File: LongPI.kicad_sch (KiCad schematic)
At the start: 10 parts, among them J1 USB_C_Receptacle_USB2.0, J2 Conn_01x30, U1 RP2040, U2 USBLC6-2SC6, U3 XC6210B332MR, U4 W25Q128JVS

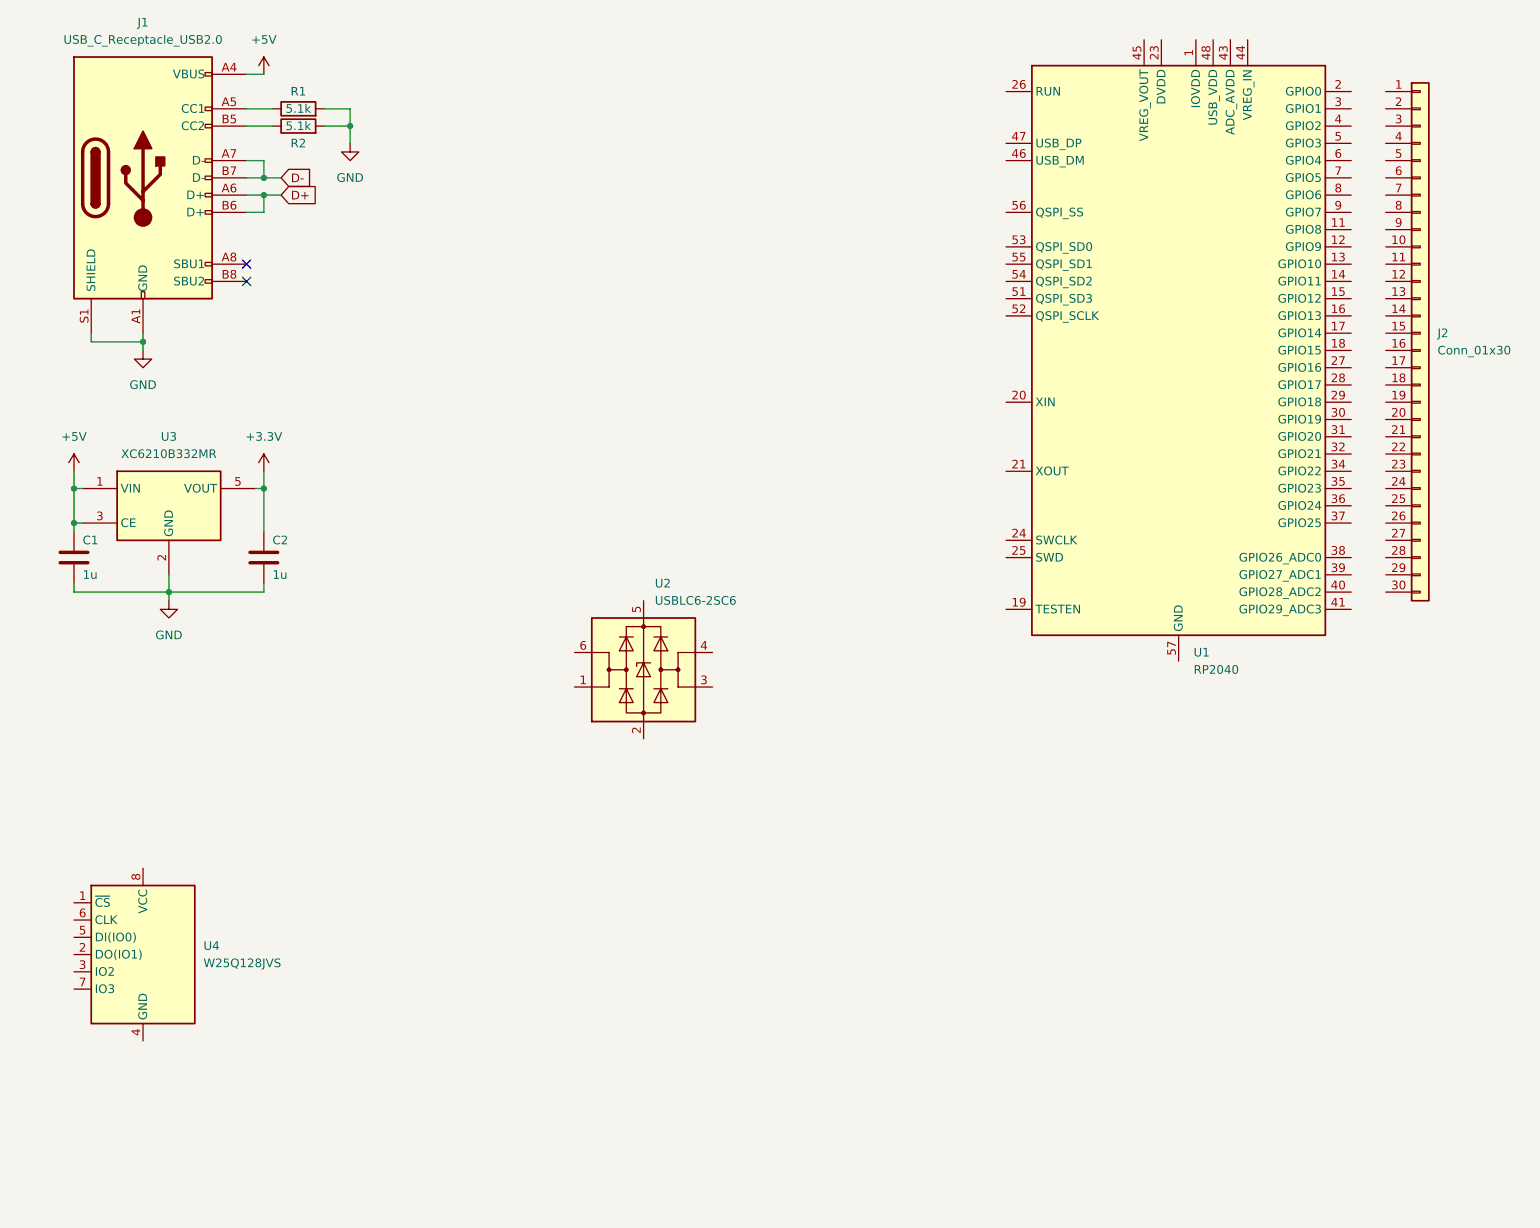
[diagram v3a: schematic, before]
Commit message: ESD protection setup on sch
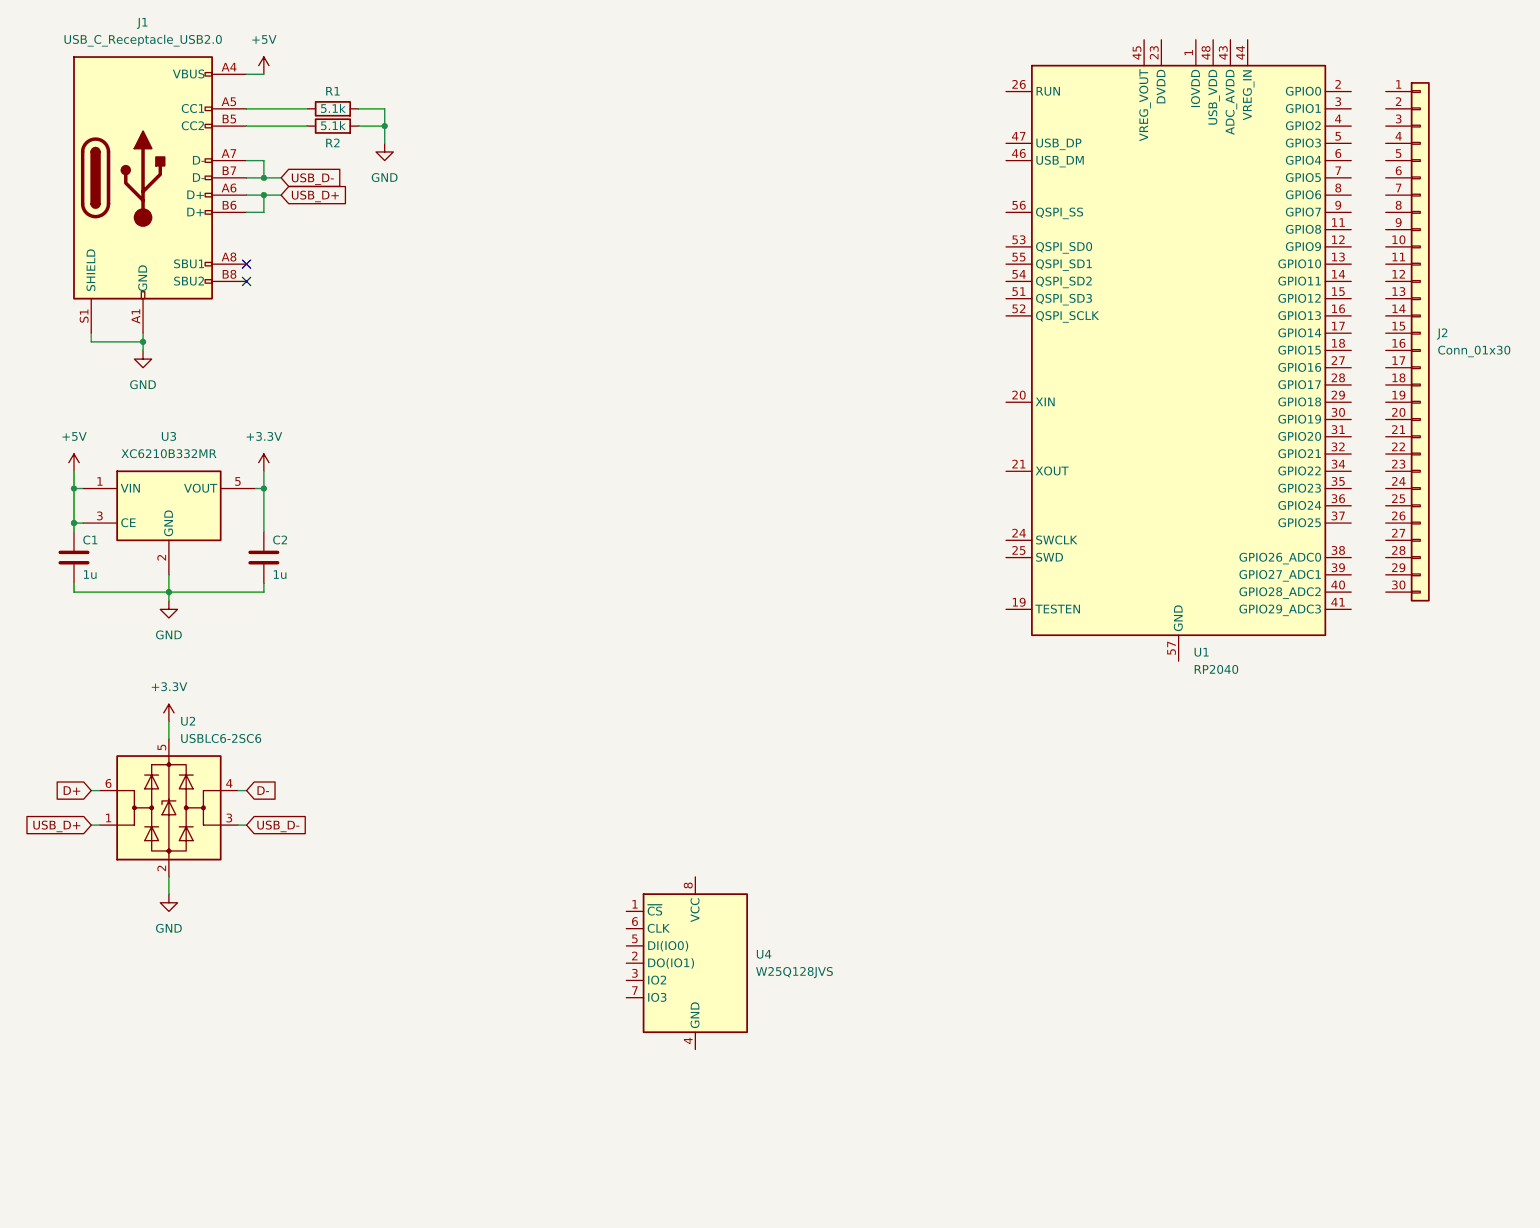
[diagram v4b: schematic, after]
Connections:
- net +3.3V: now also U2.5 (VBUS)
- net D+: now also U2.6 (I/O1); no longer J1.A6 (D+), J1.B6 (D+)
- net D-: now also U2.4 (I/O2); no longer J1.A7 (D-), J1.B7 (D-)
- net GND: now also U2.2 (GND)
- net USB_D+: now reaches U2.1 (I/O1)
- net USB_D+: now also J1.A6 (D+), J1.B6 (D+)
- net USB_D-: now reaches U2.3 (I/O2)
- net USB_D-: now also J1.A7 (D-), J1.B7 (D-)
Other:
- moved on the sheet: R1, R2, U2, U4

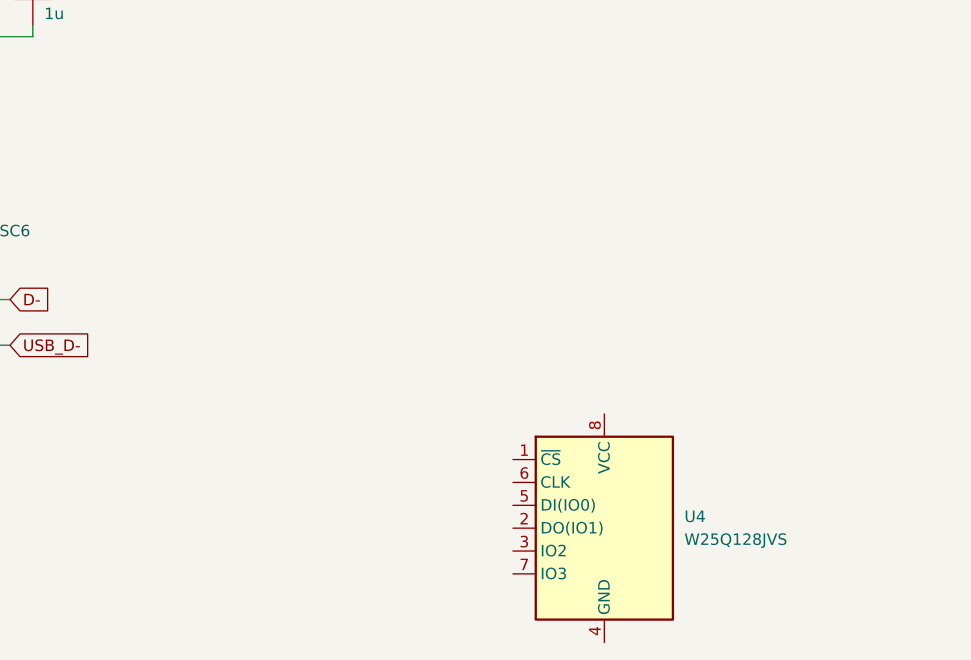
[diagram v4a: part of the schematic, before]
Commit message: Flash setup on sch
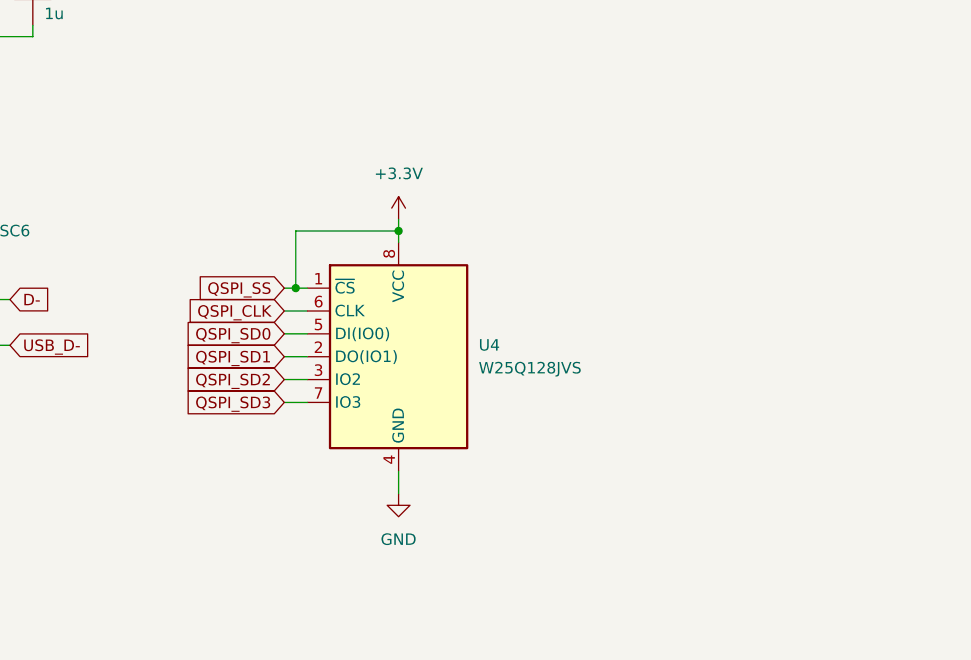
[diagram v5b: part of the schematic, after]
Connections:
- net +3.3V: now also U4.1 (~{CS}), U4.8 (VCC)
- net GND: now also U4.4 (GND)
- net QSPI_SD1: now reaches U4.2 (DO(IO1))
- net QSPI_SD2: now reaches U4.3 (IO2)
- net QSPI_SD0: now reaches U4.5 (DI(IO0))
- net QSPI_CLK: now reaches U4.6 (CLK)
- net QSPI_SD3: now reaches U4.7 (IO3)
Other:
- moved on the sheet: U4
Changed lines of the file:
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@@
   (junction (at 53.34 39.37) (diameter 0) (color 0 0 0 0)
   )
+  (junction (at 82.55 128.27) (diameter 0) (color 0 0 0 0)
+  )
   (junction (at 35.56 63.5) (diameter 0) (color 0 0 0 0)
   )
@@
   )
   (junction (at 53.34 85.09) (diameter 0) (color 0 0 0 0)
+  )
+  (junction (at 93.98 121.92) (diameter 0) (color 0 0 0 0)
   )
   (junction (at 71.12 31.75) (diameter 0) (color 0 0 0 0)
@@
     (stroke (width 0) (type default))
   )
+  (wire (pts (xy 82.55 128.27) (xy 83.82 128.27))
+    (stroke (width 0) (type default))
+  )
   (wire (pts (xy 50.8 44.45) (xy 53.34 44.45))
     (stroke (width 0) (type default))
@@
     (stroke (width 0) (type default))
   )
+  (wire (pts (xy 81.28 138.43) (xy 83.82 138.43))
+    (stroke (width 0) (type default))
+  )
   (wire (pts (xy 53.34 85.09) (xy 52.07 85.09))
     (stroke (width 0) (type default))
@@
     (stroke (width 0) (type default))
   )
+  (wire (pts (xy 81.28 128.27) (xy 82.55 128.27))
+    (stroke (width 0) (type default))
+  )
   (wire (pts (xy 25.4 91.44) (xy 25.4 90.17))
     (stroke (width 0) (type default))
@@
     (stroke (width 0) (type default))
   )
+  (wire (pts (xy 81.28 133.35) (xy 83.82 133.35))
+    (stroke (width 0) (type default))
+  )
+  (wire (pts (xy 81.28 135.89) (xy 83.82 135.89))
+    (stroke (width 0) (type default))
+  )
   (wire (pts (xy 50.8 39.37) (xy 53.34 39.37))
     (stroke (width 0) (type default))
@@
     (stroke (width 0) (type default))
   )
+  (wire (pts (xy 81.28 140.97) (xy 83.82 140.97))
+    (stroke (width 0) (type default))
+  )
   (wire (pts (xy 49.53 134.62) (xy 50.8 134.62))
     (stroke (width 0) (type default))
@@
     (stroke (width 0) (type default))
   )
+  (wire (pts (xy 93.98 120.65) (xy 93.98 121.92))
+    (stroke (width 0) (type default))
+  )
   (wire (pts (xy 50.8 31.75) (xy 59.69 31.75))
     (stroke (width 0) (type default))
@@
     (stroke (width 0) (type default))
   )
+  (wire (pts (xy 93.98 148.59) (xy 93.98 151.13))
+    (stroke (width 0) (type default))
+  )
   (wire (pts (xy 67.31 31.75) (xy 71.12 31.75))
     (stroke (width 0) (type default))
   )
+  (wire (pts (xy 81.28 130.81) (xy 83.82 130.81))
+    (stroke (width 0) (type default))
+  )
   (wire (pts (xy 39.37 119.38) (xy 39.37 121.92))
     (stroke (width 0) (type default))
@@
     (stroke (width 0) (type default))
   )
+  (wire (pts (xy 93.98 121.92) (xy 82.55 121.92))
+    (stroke (width 0) (type default))
+  )
+  (wire (pts (xy 93.98 121.92) (xy 93.98 123.19))
+    (stroke (width 0) (type default))
+  )
   (wire (pts (xy 25.4 100.33) (xy 39.37 100.33))
     (stroke (width 0) (type default))
@@
     (stroke (width 0) (type default))
   )
+  (wire (pts (xy 82.55 121.92) (xy 82.55 128.27))
+    (stroke (width 0) (type default))
+  )
   (wire (pts (xy 50.8 36.83) (xy 53.34 36.83))
     (stroke (width 0) (type default))
+  )
+  (global_label "QSPI_CLK" (shape input) (at 81.28 130.81 180) (fields_autoplaced)
+    (effects (font (size 1.27 1.27)) (justify right))
+    (property "Intersheetrefs" "${INTERSHEET_REFS}" (at 69.3443 130.81 0)
+      (effects (font (size 1.27 1.27)) (justify right) hide)
+    )
   )
   (global_label "D-" (shape input) (at 50.8 129.54 0) (fields_autoplaced)
@@
     )
   )
+  (global_label "QSPI_SD2" (shape input) (at 81.28 138.43 180) (fields_autoplaced)
+    (effects (font (size 1.27 1.27)) (justify right))
+    (property "Intersheetrefs" "${INTERSHEET_REFS}" (at 69.2234 138.43 0)
+      (effects (font (size 1.27 1.27)) (justify right) hide)
+    )
+  )
+  (global_label "QSPI_SD1" (shape input) (at 81.28 135.89 180) (fields_autoplaced)
+    (effects (font (size 1.27 1.27)) (justify right))
+    (property "Intersheetrefs" "${INTERSHEET_REFS}" (at 69.2234 135.89 0)
+      (effects (font (size 1.27 1.27)) (justify right) hide)
+    )
+  )
+  (global_label "QSPI_SD0" (shape input) (at 81.28 133.35 180) (fields_autoplaced)
+    (effects (font (size 1.27 1.27)) (justify right))
+    (property "Intersheetrefs" "${INTERSHEET_REFS}" (at 69.2234 133.35 0)
+      (effects (font (size 1.27 1.27)) (justify right) hide)
+    )
+  )
   (global_label "USB_D+" (shape input) (at 27.94 134.62 180) (fields_autoplaced)
     (effects (font (size 1.27 1.27)) (justify right))
@@
     )
   )
+  (global_label "QSPI_SD3" (shape input) (at 81.28 140.97 180) (fields_autoplaced)
+    (effects (font (size 1.27 1.27)) (justify right))
+    (property "Intersheetrefs" "${INTERSHEET_REFS}" (at 69.2234 140.97 0)
+      (effects (font (size 1.27 1.27)) (justify right) hide)
+    )
+  )
+  (global_label "QSPI_SS" (shape input) (at 81.28 128.27 180) (fields_autoplaced)
+    (effects (font (size 1.27 1.27)) (justify right))
+    (property "Intersheetrefs" "${INTERSHEET_REFS}" (at 70.4934 128.27 0)
+      (effects (font (size 1.27 1.27)) (justify right) hide)
+    )
+  )
   (global_label "USB_D-" (shape input) (at 55.88 39.37 0) (fields_autoplaced)
     (effects (font (size 1.27 1.27)) (justify left))
@@
     )
   )
+  (symbol (lib_id "power:+3.3V") (at 93.98 120.65 0) (unit 1)
+    (in_bom yes) (on_board yes) (dnp no) (fields_autoplaced)
+    (property "Reference" "#PWR09" (at 93.98 124.46 0)
+      (effects (font (size 1.27 1.27)) hide)
+    )
+    (property "Value" "+3.3V" (at 93.98 115.57 0)
+      (effects (font (size 1.27 1.27)))
+    )
+    (property "Footprint" "" (at 93.98 120.65 0)
+      (effects (font (size 1.27 1.27)) hide)
+    )
+    (property "Datasheet" "" (at 93.98 120.65 0)
+      (effects (font (size 1.27 1.27)) hide)
+    )
+    (pin "1")
+    (instances
+      (project "LongPI"
+        (path "/cc33761c-f139-4a76-bdf7-f72d959ddb3d"
+          (reference "#PWR09") (unit 1)
+        )
+      )
+    )
+  )
   (symbol (lib_id "power:+5V") (at 25.4 82.55 0) (unit 1)
     (in_bom yes) (on_board yes) (dnp no) (fields_autoplaced)
@@
     )
   )
-  (symbol (lib_id "Memory_Flash:W25Q128JVS") (at 116.84 154.94 0) (unit 1)
-    (in_bom yes) (on_board yes) (dnp no) (fields_autoplaced)
-    (property "Reference" "U4" (at 125.73 153.67 0)
-      (effects (font (size 1.27 1.27)) (justify left))
-    )
-    (property "Value" "W25Q128JVS" (at 125.73 156.21 0)
-      (effects (font (size 1.27 1.27)) (justify left))
-    )
-    (property "Footprint" "Package_SO:SOIC-8_5.23x5.23mm_P1.27mm" (at 116.84 154.94 0)
-      (effects (font (size 1.27 1.27)) hide)
-    )
-    (property "Datasheet" "http://www.winbond.com/resource-files/w25q128jv_dtr%20revc%2003272018%20plus.pdf" (at 116.84 154.94 0)
+  (symbol (lib_id "Memory_Flash:W25Q128JVS") (at 93.98 135.89 0) (unit 1)
+    (in_bom yes) (on_board yes) (dnp no) (fields_autoplaced)
+    (property "Reference" "U4" (at 102.87 134.62 0)
+      (effects (font (size 1.27 1.27)) (justify left))
+    )
+    (property "Value" "W25Q128JVS" (at 102.87 137.16 0)
+      (effects (font (size 1.27 1.27)) (justify left))
+    )
+    (property "Footprint" "Package_SO:SOIC-8_5.23x5.23mm_P1.27mm" (at 93.98 135.89 0)
+      (effects (font (size 1.27 1.27)) hide)
+    )
+    (property "Datasheet" "http://www.winbond.com/resource-files/w25q128jv_dtr%20revc%2003272018%20plus.pdf" (at 93.98 135.89 0)
       (effects (font (size 1.27 1.27)) hide)
     )
@@
         )
       )
+    )
+  )
+  (symbol (lib_id "power:GND") (at 93.98 151.13 0) (unit 1)
+    (in_bom yes) (on_board yes) (dnp no) (fields_autoplaced)
+    (property "Reference" "#PWR010" (at 93.98 157.48 0)
+      (effects (font (size 1.27 1.27)) hide)
+    )
+    (property "Value" "GND" (at 93.98 156.21 0)
+      (effects (font (size 1.27 1.27)))
+    )
+    (property "Footprint" "" (at 93.98 151.13 0)
+      (effects (font (size 1.27 1.27)) hide)
+    )
+    (property "Datasheet" "" (at 93.98 151.13 0)
+      (effects (font (size 1.27 1.27)) hide)
+    )
+    (pin "1")
+    (instances
+      (project "LongPI"
+        (path "/cc33761c-f139-4a76-bdf7-f72d959ddb3d"
+          (reference "#PWR010") (unit 1)
+        )
+      )
